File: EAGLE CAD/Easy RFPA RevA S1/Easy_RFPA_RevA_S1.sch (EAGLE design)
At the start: 197 parts, among them J101 COAX112640BNC_EDGE, J102 COAX112640BNC_EDGE, J301 COAX112640BNC_EDGE, J302 COAX112640BNC_EDGE, J401 HDR_2X1282836-1282836-1, J402 KK_PCFAN, Q101 IRF520N, Q102 IRF520N, Q201 IRF630, Q202 IRF630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

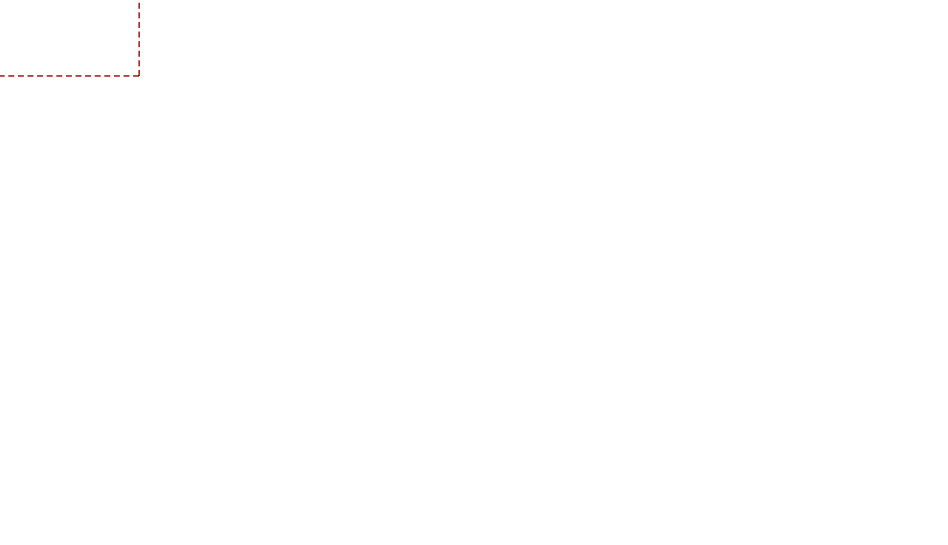
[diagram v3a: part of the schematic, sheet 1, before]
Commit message: Add global attributes and sheet names
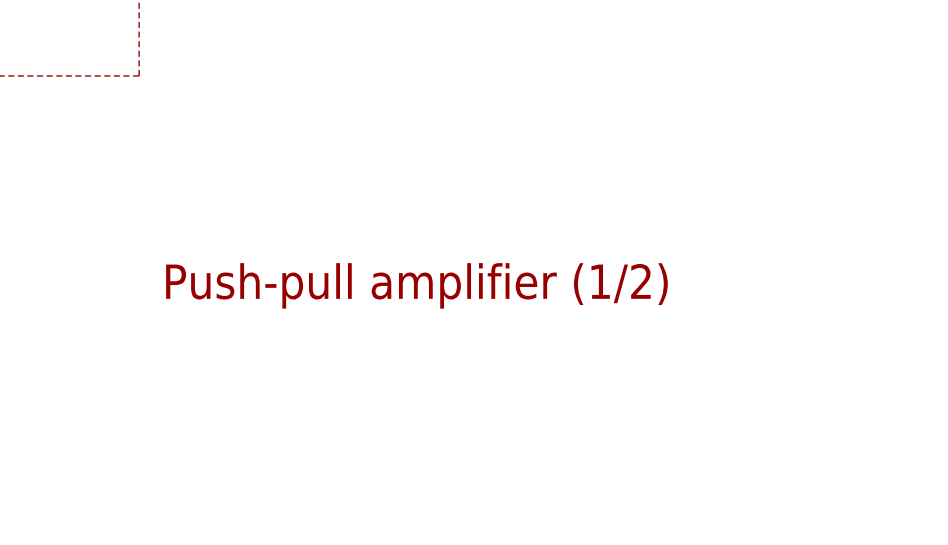
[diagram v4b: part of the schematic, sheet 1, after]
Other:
- note added: "Gate Bias Control"
- note added: "Power Entry"
- note added: "Push-pull amplifier (1/2)"
- note added: "Push-pull amplifier (2/2)"
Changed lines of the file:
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@@
 <schematic xreflabel="%F%N" xrefpart="/%S.%C%R">
 <attributes>
+<attribute name="AUTHOR" value="MDT"/>
+<attribute name="BOMREV" value="01"/>
+<attribute name="DRAWING_NUMBER" value=" "/>
+<attribute name="FABREV" value="A"/>
 </attributes>
 <variantdefs>
@@
 Max duty cycle: 3.5% (500us, 70Hz rep rate, passive convection)
 Max pulse width: 1ms</text>
+<text x="327.66" y="27.94" size="3.81" layer="94" align="center-left">Push-pull amplifier (1/2)</text>
 </plain>
 <instances>
@@
 Max duty cycle: 3.5% (500us, 70Hz rep rate, passive convection)
 Max pulse width: 1ms</text>
+<text x="327.66" y="27.94" size="3.81" layer="94" align="center-left">Push-pull amplifier (2/2)</text>
 </plain>
 <instances>
@@
 Max duty cycle: 3.5% (500us, 70Hz rep rate, passive convection)
 Max pulse width: 1ms</text>
+<text x="327.66" y="27.94" size="3.81" layer="94" align="center-left">Gate Bias Control</text>
 </plain>
 <instances>
@@
 Max pulse width: 1ms</text>
 <text x="375.92" y="137.16" size="2.54" layer="94" align="center">Thermal pads and heatsink clips</text>
+<text x="327.66" y="27.94" size="3.81" layer="94" align="center-left">Power Entry</text>
 </plain>
 <instances>

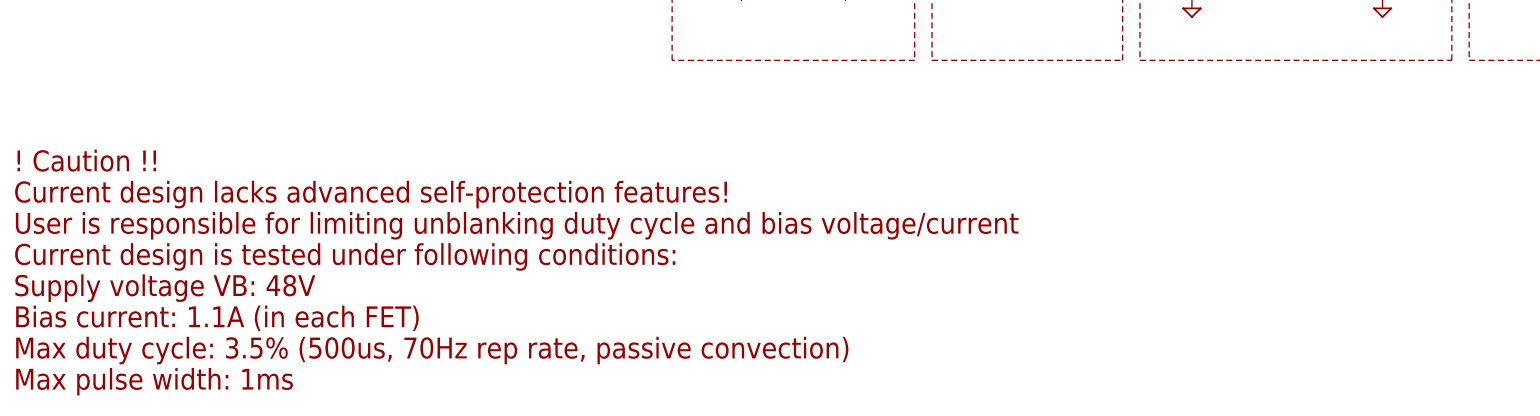
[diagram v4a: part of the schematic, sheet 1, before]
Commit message: Replace frames and re-print pdfs
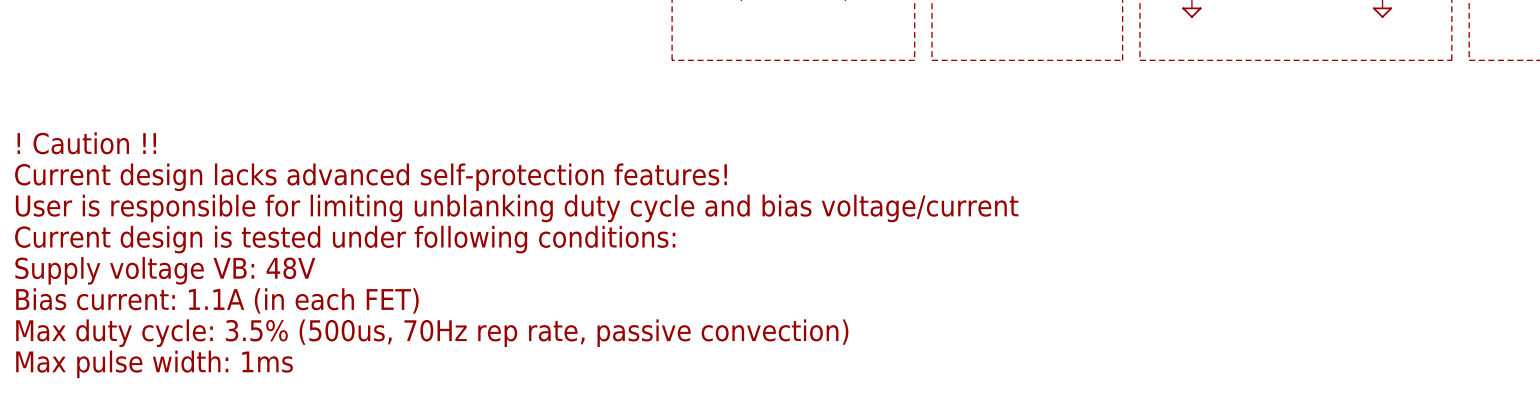
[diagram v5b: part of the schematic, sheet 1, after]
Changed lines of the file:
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@@
 <parts>
 <part name="Q101" library="MDT_TRANS" deviceset="MOSFET_N" device="TO-220-VERT" technology="IRF520N" value="IRF520N"/>
-<part name="FRAME301" library="frames" deviceset="FRAME_B_L" device=""/>
-<part name="FRAME101" library="frames" deviceset="FRAME_B_L" device=""/>
 <part name="U302" library="MDT_IC" deviceset="OPAMP_QUAD" device="SOIC14" technology="TLV274ID" value="OPAMP_QUADTLV274IDSOIC14"/>
 <part name="Q303" library="MDT_TRANS" deviceset="NPN" device="SOT23_BEC" technology="MMBT3904"/>
@@
 <part name="JP302" library="pinhead" deviceset="PINHD-1X2" device=""/>
 <part name="JP301" library="pinhead" deviceset="PINHD-1X2" device=""/>
-<part name="FRAME401" library="frames" deviceset="FRAME_B_L" device=""/>
 <part name="U401" library="MDT_IC" deviceset="LDO_3TERM" device="TO220_VERT" technology="MC78M12CTG" value="LDO_3TERMMC78M12CTGTO220_VERT"/>
 <part name="U402" library="MDT_IC" deviceset="LDO_3TERM" device="TO220_VERT" technology="MC78M05CTG" value="LDO_3TERMMC78M05CTGTO220_VERT"/>
@@
 <part name="C409" library="MDT_C" deviceset="CPOL" device="E2,5-7" technology="C-22U-63V-20%-6.3DX12.5L-ELEC" value="22uF"/>
 <part name="SUPPLY413" library="supply2" deviceset="GND" device=""/>
-<part name="FRAME201" library="frames" deviceset="FRAME_B_L" device=""/>
 <part name="L103" library="MDT_L" deviceset="L" device="" technology="L-22U-FERRITE-20%-12.5X12.5MM-4A" value="22uH">
 <variant name="IRF520N_20W"/>
@@
 <part name="X407" library="MDT_HEATSINK" deviceset="HEATSINK_CLIP" device="" technology="OMNI-220C"/>
 <part name="X409" library="MDT_HEATSINK" deviceset="HEATSINK_CLIP" device="" technology="OMNI-220C"/>
+<part name="FRAME1" library="MDT_frames" deviceset="FRAME_B_L" device=""/>
+<part name="FRAME2" library="MDT_frames" deviceset="FRAME_B_L" device=""/>
+<part name="FRAME3" library="MDT_frames" deviceset="FRAME_B_L" device=""/>
+<part name="FRAME4" library="MDT_frames" deviceset="FRAME_B_L" device=""/>
 </parts>
 <sheets>
@@
 <text x="58.42" y="203.2" size="2.54" layer="94" align="center">Input balun</text>
 <text x="378.46" y="208.28" size="2.54" layer="94" align="center">Output balun</text>
-<text x="7.62" y="2.54" size="3.048" layer="94">! Caution !!
+<text x="7.62" y="5.08" size="3.048" layer="94">! Caution !!
 Current design lacks advanced self-protection features!
 User is responsible for limiting unblanking duty cycle and bias voltage/current
@@
 <instances>
 <instance part="Q101" gate="G$1" x="264.16" y="182.88"/>
-<instance part="FRAME101" gate="G$1" x="0" y="0"/>
-<instance part="FRAME101" gate="G$2" x="325.12" y="0"/>
 <instance part="Q102" gate="G$1" x="264.16" y="83.82"/>
 <instance part="SUPPLY123" gate="GND" x="264.16" y="58.42" smashed="yes"/>
@@
 <instance part="L103" gate="G$1" x="292.1" y="208.28" rot="R90"/>
 <instance part="L104" gate="G$1" x="294.64" y="109.22" rot="R90"/>
+<instance part="FRAME1" gate="G$1" x="0" y="0"/>
+<instance part="FRAME1" gate="G$2" x="325.12" y="0"/>
 </instances>
 <busses>
@@
 <text x="195.58" y="119.38" size="2.54" layer="94" align="center">Gate damping</text>
 <text x="241.3" y="218.44" size="2.54" layer="94" align="center">Power FET</text>
-<text x="238.76" y="119.38" size="2.54" layer="94" align="center">Power FET</text>
+<text x="241.3" y="119.38" size="2.54" layer="94" align="center">Power FET</text>
 <text x="7.62" y="5.08" size="3.048" layer="94">! Caution !!
 Current design lacks advanced self-protection features!
@@
 <instance part="TP17" gate="G$1" x="317.5" y="73.66" rot="MR0"/>
 <instance part="SUPPLY226" gate="GND" x="312.42" y="66.04" smashed="yes"/>
-<instance part="FRAME201" gate="G$1" x="0" y="0"/>
-<instance part="FRAME201" gate="G$2" x="325.12" y="0"/>
+<instance part="FRAME2" gate="G$1" x="0" y="0"/>
+<instance part="FRAME2" gate="G$2" x="325.12" y="0"/>
 </instances>
 <busses>
@@
 </plain>
 <instances>
-<instance part="FRAME301" gate="G$1" x="0" y="0"/>
-<instance part="FRAME301" gate="G$2" x="325.12" y="0"/>
 <instance part="U302" gate="A" x="266.7" y="175.26"/>
 <instance part="Q303" gate="G$1" x="309.88" y="185.42"/>
@@
 <instance part="R309" gate="G$1" x="152.4" y="101.6"/>
 <instance part="R304" gate="G$1" x="99.06" y="93.98"/>
+<instance part="FRAME3" gate="G$1" x="0" y="0"/>
+<instance part="FRAME3" gate="G$2" x="325.12" y="0"/>
 </instances>
 <busses>
@@
 </plain>
 <instances>
-<instance part="FRAME401" gate="G$1" x="0" y="0"/>
-<instance part="FRAME401" gate="G$2" x="325.12" y="0"/>
 <instance part="U401" gate="G$1" x="198.12" y="137.16"/>
 <instance part="U402" gate="G$1" x="198.12" y="101.6"/>
@@
 <instance part="X407" gate="G$1" x="365.76" y="116.84"/>
 <instance part="X409" gate="G$1" x="398.78" y="116.84"/>
+<instance part="FRAME4" gate="G$1" x="0" y="0"/>
+<instance part="FRAME4" gate="G$2" x="325.12" y="0"/>
 </instances>
 <busses>
